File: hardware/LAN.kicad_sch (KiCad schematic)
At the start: 28 parts, among them J4 RJ45_Hanrun_HR911105A_Horizon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, U4 W5500, Y2 XO32F025000GEHE001

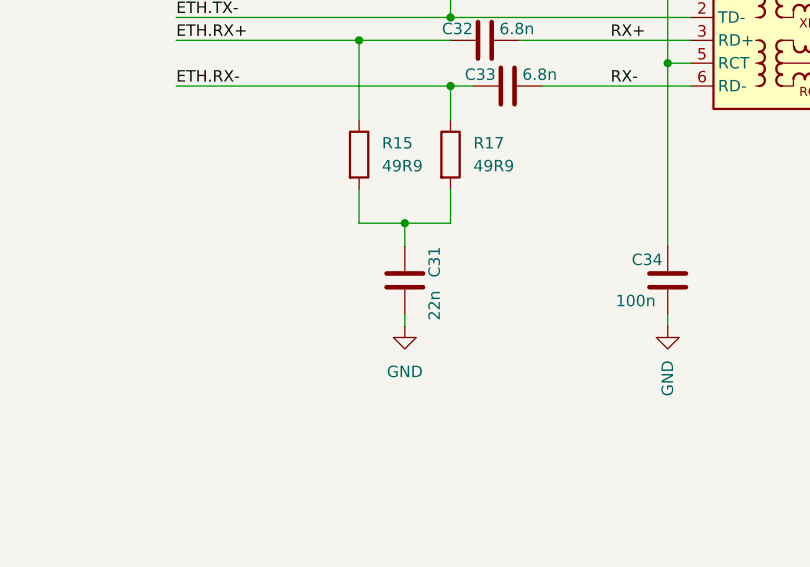
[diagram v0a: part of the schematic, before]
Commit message: feat: add SWD footprint
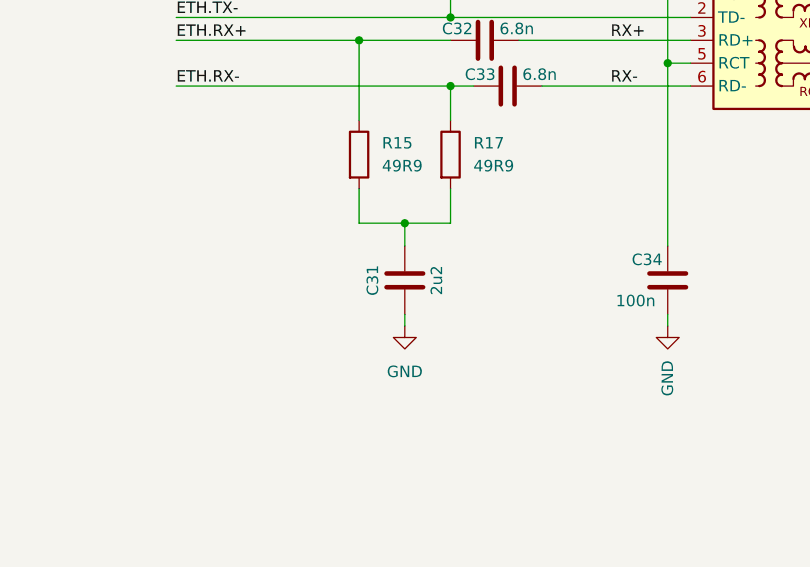
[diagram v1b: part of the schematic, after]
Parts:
- C31: value 22n -> 2u2; footprint Capacitor_SMD:C_0603_1608Metric -> Hardware Components:C_0402_1005Metric; symbol Device:C -> Hardware Components:C_2u2_0402_25V; JLCPCB Part # C57895 -> C307418; MPN CL10A225KA8NNNC -> CL05A225KA5NUNC
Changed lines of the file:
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@@
 	)
 	(symbol
-		(lib_id "Device:C")
+		(lib_id "Hardware Components:C_2u2_0402_25V")
 		(at 170.18 97.79 0)
 		(unit 1)
@@
 		(dnp no)
 		(property "Reference" "C31"
-			(at 173.482 95.758 90)
+			(at 166.624 97.79 90)
 			(effects
 				(font
@@
 			)
 		)
-		(property "Value" "22n"
-			(at 173.482 100.584 90)
+		(property "Value" "2u2"
+			(at 173.736 97.79 90)
 			(effects
 				(font
@@
 			)
 		)
-		(property "Footprint" "Capacitor_SMD:C_0603_1608Metric"
+		(property "Footprint" "Hardware Components:C_0402_1005Metric"
+			(at 171.1452 101.6 0)
+			(effects
+				(font
+					(size 1.27 1.27)
+				)
+				(hide yes)
+			)
+		)
+		(property "Datasheet" "https://jlcpcb.com/api/file/downloadByFileSystemAccessId/8588894249148014592"
+			(at 170.18 97.79 0)
+			(effects
+				(font
+					(size 1.27 1.27)
+				)
+				(hide yes)
+			)
+		)
+		(property "Description" "2.2uF 25V X5R ±10% 0402 Multilayer Ceramic Capacitors MLCC - SMD/SMT ROHS"
+			(at 170.18 97.79 0)
+			(effects
+				(font
+					(size 1.27 1.27)
+				)
+				(hide yes)
+			)
+		)
+		(property "MPN" "CL05A225KA5NUNC"
 			(at 170.18 97.79 90)
 			(effects
@@
 			)
 		)
-		(property "Datasheet" "https://jlcpcb.com/api/file/downloadByFileSystemAccessId/8586178788720332800"
+		(property "JLCPCB Part #" "C307418"
 			(at 170.18 97.79 90)
 			(effects
-				(font
-					(size 1.27 1.27)
-				)
-				(hide yes)
-			)
-		)
-		(property "Description" "25V 2.2uF X5R ±10% 0603 Multilayer Ceramic Capacitors MLCC - SMD/SMT ROHS"
-			(at 170.18 97.79 0)
-			(effects
-				(font
-					(size 1.27 1.27)
-				)
-				(hide yes)
-			)
-		)
-		(property "MPN" "CL10A225KA8NNNC"
-			(at 170.18 97.79 90)
-			(effects
-				(font
-					(size 1.27 1.27)
-				)
-				(hide yes)
-			)
-		)
-		(property "JLCPCB Part #" "C57895"
-			(at 170.18 97.79 90)
-			(effects
